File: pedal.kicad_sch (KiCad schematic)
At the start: 0 parts

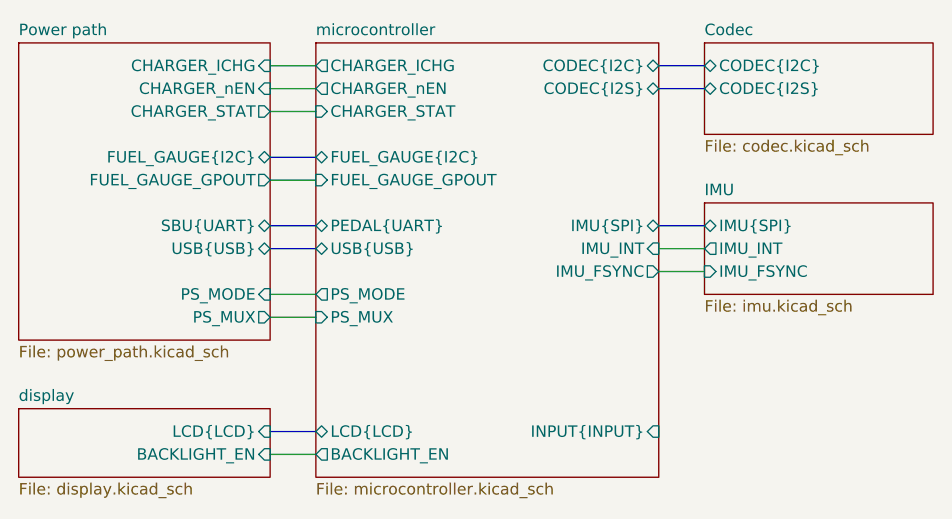
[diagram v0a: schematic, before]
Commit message: Replace output amp with TPA6130A2
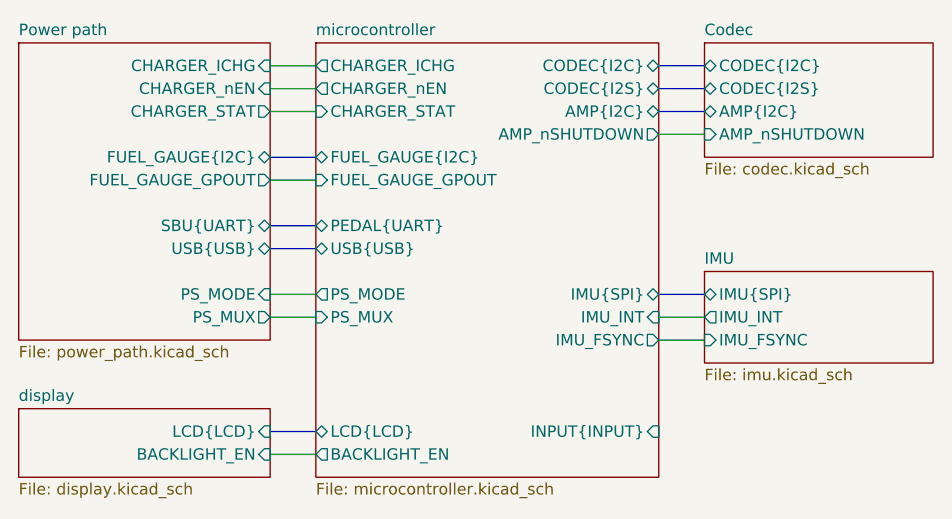
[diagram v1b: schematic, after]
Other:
- sheet Codec ports: added AMP_nSHUTDOWN, AMP{I2C}; removed none
- sheet microcontroller ports: added AMP_nSHUTDOWN, AMP{I2C}; removed none
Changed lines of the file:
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@@
 	(bus
 		(pts
-			(xy 167.64 91.44) (xy 172.72 91.44)
+			(xy 167.64 99.06) (xy 172.72 99.06)
 		)
 		(stroke
@@
 	(wire
 		(pts
-			(xy 167.64 96.52) (xy 172.72 96.52)
+			(xy 167.64 104.14) (xy 172.72 104.14)
+		)
+		(stroke
+			(width 0)
+			(type default)
+		)
+	)
+	(bus
+		(pts
+			(xy 167.64 78.74) (xy 172.72 78.74)
 		)
 		(stroke
@@
 	(wire
 		(pts
-			(xy 167.64 93.98) (xy 172.72 93.98)
+			(xy 167.64 101.6) (xy 172.72 101.6)
 		)
 		(stroke
@@
 		(pts
 			(xy 124.46 78.74) (xy 129.54 78.74)
+		)
+		(stroke
+			(width 0)
+			(type default)
+		)
+	)
+	(wire
+		(pts
+			(xy 167.64 81.28) (xy 172.72 81.28)
 		)
 		(stroke
@@
 	)
 	(sheet
-		(at 172.72 88.9)
+		(at 172.72 96.52)
 		(size 25.4 10.16)
 		(exclude_from_sim no)
@@
 		)
 		(property "Sheetname" "IMU"
-			(at 172.72 88.1884 0)
+			(at 172.72 95.8084 0)
 			(show_name no)
 			(do_not_autoplace no)
@@
 		)
 		(property "Sheetfile" "imu.kicad_sch"
-			(at 172.72 99.6446 0)
+			(at 172.72 107.2646 0)
 			(show_name no)
 			(do_not_autoplace no)
@@
 		)
 		(pin "IMU_FSYNC" input
-			(at 172.72 96.52 180)
+			(at 172.72 104.14 180)
 			(effects
 				(font
@@
 		)
 		(pin "IMU_INT" output
-			(at 172.72 93.98 180)
+			(at 172.72 101.6 180)
 			(effects
 				(font
@@
 		)
 		(pin "IMU{SPI}" bidirectional
-			(at 172.72 91.44 180)
+			(at 172.72 99.06 180)
 			(effects
 				(font
@@
 	(sheet
 		(at 172.72 71.12)
-		(size 25.4 10.16)
+		(size 25.4 12.7)
 		(exclude_from_sim no)
 		(in_bom yes)
@@
 		)
 		(property "Sheetfile" "codec.kicad_sch"
-			(at 172.72 81.8646 0)
+			(at 172.72 84.4046 0)
 			(show_name no)
 			(do_not_autoplace no)
@@
 		(pin "CODEC{I2S}" bidirectional
 			(at 172.72 76.2 180)
+			(effects
+				(font
+					(size 1.27 1.27)
+				)
+				(justify left)
+			)
+		)
+		(pin "AMP_nSHUTDOWN" input
+			(at 172.72 81.28 180)
+			(effects
+				(font
+					(size 1.27 1.27)
+				)
+				(justify left)
+			)
+		)
+		(pin "AMP{I2C}" bidirectional
+			(at 172.72 78.74 180)
 			(effects
 				(font
@@
 		)
 		(pin "IMU_FSYNC" output
-			(at 167.64 96.52 0)
+			(at 167.64 104.14 0)
 			(effects
 				(font
@@
 		)
 		(pin "IMU_INT" input
-			(at 167.64 93.98 0)
+			(at 167.64 101.6 0)
 			(effects
 				(font
@@
 		)
 		(pin "IMU{SPI}" bidirectional
-			(at 167.64 91.44 0)
+			(at 167.64 99.06 0)
 			(effects
 				(font
@@
 			)
 		)
+		(pin "AMP_nSHUTDOWN" output
+			(at 167.64 81.28 0)
+			(effects
+				(font
+					(size 1.27 1.27)
+				)
+				(justify right)
+			)
+		)
+		(pin "AMP{I2C}" bidirectional
+			(at 167.64 78.74 0)
+			(effects
+				(font
+					(size 1.27 1.27)
+				)
+				(justify right)
+			)
+		)

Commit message: FINALLY add 3.5mm audio jacks
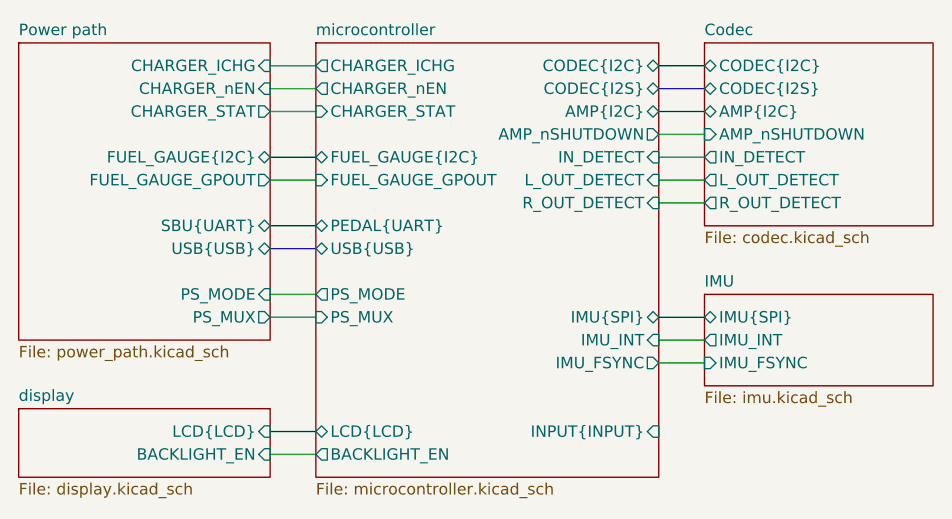
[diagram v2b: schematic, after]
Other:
- sheet Codec ports: added IN_DETECT, L_OUT_DETECT, R_OUT_DETECT; removed none
- sheet microcontroller ports: added IN_DETECT, L_OUT_DETECT, R_OUT_DETECT; removed none
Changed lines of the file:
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@@
 	(bus
 		(pts
-			(xy 167.64 99.06) (xy 172.72 99.06)
+			(xy 167.64 101.6) (xy 172.72 101.6)
 		)
 		(stroke
@@
 	(wire
 		(pts
+			(xy 167.64 106.68) (xy 172.72 106.68)
+		)
+		(stroke
+			(width 0)
+			(type default)
+		)
+	)
+	(bus
+		(pts
+			(xy 167.64 78.74) (xy 172.72 78.74)
+		)
+		(stroke
+			(width 0)
+			(type default)
+		)
+	)
+	(bus
+		(pts
+			(xy 124.46 114.3) (xy 129.54 114.3)
+		)
+		(stroke
+			(width 0)
+			(type default)
+		)
+	)
+	(wire
+		(pts
 			(xy 167.64 104.14) (xy 172.72 104.14)
 		)
@@
 		)
 	)
+	(wire
+		(pts
+			(xy 167.64 86.36) (xy 172.72 86.36)
+		)
+		(stroke
+			(width 0)
+			(type default)
+		)
+	)
 	(bus
 		(pts
-			(xy 167.64 78.74) (xy 172.72 78.74)
+			(xy 124.46 93.98) (xy 129.54 93.98)
+		)
+		(stroke
+			(width 0)
+			(type default)
+		)
+	)
+	(wire
+		(pts
+			(xy 124.46 78.74) (xy 129.54 78.74)
+		)
+		(stroke
+			(width 0)
+			(type default)
+		)
+	)
+	(wire
+		(pts
+			(xy 167.64 83.82) (xy 172.72 83.82)
+		)
+		(stroke
+			(width 0)
+			(type default)
+		)
+	)
+	(wire
+		(pts
+			(xy 167.64 81.28) (xy 172.72 81.28)
 		)
 		(stroke
@@
 	(bus
 		(pts
-			(xy 124.46 114.3) (xy 129.54 114.3)
-		)
-		(stroke
-			(width 0)
-			(type default)
-		)
-	)
-	(wire
-		(pts
-			(xy 167.64 101.6) (xy 172.72 101.6)
+			(xy 167.64 76.2) (xy 172.72 76.2)
 		)
 		(stroke
@@
 	(bus
 		(pts
-			(xy 124.46 93.98) (xy 129.54 93.98)
-		)
-		(stroke
-			(width 0)
-			(type default)
-		)
-	)
-	(wire
-		(pts
-			(xy 124.46 78.74) (xy 129.54 78.74)
-		)
-		(stroke
-			(width 0)
-			(type default)
-		)
-	)
-	(wire
-		(pts
-			(xy 167.64 81.28) (xy 172.72 81.28)
-		)
-		(stroke
-			(width 0)
-			(type default)
-		)
-	)
-	(bus
-		(pts
-			(xy 167.64 76.2) (xy 172.72 76.2)
-		)
-		(stroke
-			(width 0)
-			(type default)
-		)
-	)
-	(bus
-		(pts
 			(xy 124.46 91.44) (xy 129.54 91.44)
 		)
@@
 		(pts
 			(xy 124.46 86.36) (xy 129.54 86.36)
+		)
+		(stroke
+			(width 0)
+			(type default)
+		)
+	)
+	(wire
+		(pts
+			(xy 167.64 88.9) (xy 172.72 88.9)
 		)
 		(stroke
@@
 	)
 	(sheet
-		(at 172.72 96.52)
+		(at 172.72 99.06)
 		(size 25.4 10.16)
 		(exclude_from_sim no)
@@
 		)
 		(property "Sheetname" "IMU"
-			(at 172.72 95.8084 0)
+			(at 172.72 98.3484 0)
 			(show_name no)
 			(do_not_autoplace no)
@@
 		)
 		(property "Sheetfile" "imu.kicad_sch"
-			(at 172.72 107.2646 0)
+			(at 172.72 109.8046 0)
 			(show_name no)
 			(do_not_autoplace no)
@@
 		)
 		(pin "IMU_FSYNC" input
+			(at 172.72 106.68 180)
+			(effects
+				(font
+					(size 1.27 1.27)
+				)
+				(justify left)
+			)
+		)
+		(pin "IMU_INT" output
 			(at 172.72 104.14 180)
 			(effects
@@
 			)
 		)
-		(pin "IMU_INT" output
+		(pin "IMU{SPI}" bidirectional
 			(at 172.72 101.6 180)
-			(effects
-				(font
-					(size 1.27 1.27)
-				)
-				(justify left)
-			)
-		)
-		(pin "IMU{SPI}" bidirectional
-			(at 172.72 99.06 180)
 			(effects
 				(font
@@
 	(sheet
 		(at 172.72 71.12)
-		(size 25.4 12.7)
+		(size 25.4 20.32)
 		(exclude_from_sim no)
 		(in_bom yes)
@@
 		)
 		(property "Sheetfile" "codec.kicad_sch"
-			(at 172.72 84.4046 0)
+			(at 172.72 92.0246 0)
 			(show_name no)
 			(do_not_autoplace no)
@@
 		(pin "AMP{I2C}" bidirectional
 			(at 172.72 78.74 180)
+			(effects
+				(font
+					(size 1.27 1.27)
+				)
+				(justify left)
+			)
+		)
+		(pin "IN_DETECT" output
+			(at 172.72 83.82 180)
+			(effects
+				(font
+					(size 1.27 1.27)
+				)
+				(justify left)
+			)
+		)
+		(pin "L_OUT_DETECT" output
+			(at 172.72 86.36 180)
+			(effects
+				(font
+					(size 1.27 1.27)
+				)
+				(justify left)
+			)
+		)
+		(pin "R_OUT_DETECT" output
+			(at 172.72 88.9 180)
 			(effects
 				(font
@@
 		)
 		(pin "IMU_FSYNC" output
+			(at 167.64 106.68 0)
+			(effects
+				(font
+					(size 1.27 1.27)
+				)
+				(justify right)
+			)
+		)
+		(pin "IMU_INT" input
 			(at 167.64 104.14 0)
 			(effects
@@
 			)
 		)
-		(pin "IMU_INT" input
+		(pin "IMU{SPI}" bidirectional
 			(at 167.64 101.6 0)
-			(effects
-				(font
-					(size 1.27 1.27)
-				)
-				(justify right)
-			)
-		)
-		(pin "IMU{SPI}" bidirectional
-			(at 167.64 99.06 0)
 			(effects
 				(font
@@
 			(effects
 				(font
+					(size 1.27 1.27)
+				)
+				(justify right)
+			)
+		)
+		(pin "IN_DETECT" input
+			(at 167.64 83.82 0)
+			(effects
+				(font
+					(size 1.27 1.27)
+				)
+				(justify right)
+			)
+		)
+		(pin "L_OUT_DETECT" input
+			(at 167.64 86.36 0)
+			(effects
+				(font
+					(size 1.27 1.27)
+				)
+				(justify right)
+			)
+		)
+		(pin "R_OUT_DETECT" input
+			(at 167.64 88.9 0)
+			(effects
+				(font

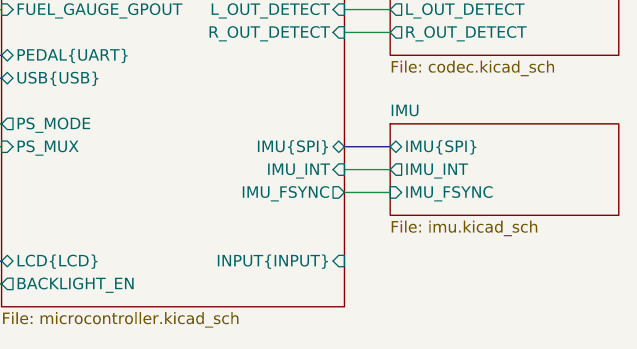
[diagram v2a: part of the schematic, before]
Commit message: Input (#6)
* Add input subsheet
* Add debounce subsheet
* Add ultra thin buttons for ABXY
* Add start and select buttons
* Add L/R buttons
* Add joystick connector
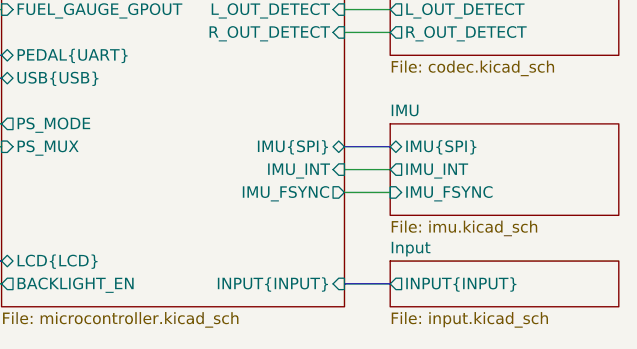
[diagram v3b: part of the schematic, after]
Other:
- added sheet Input (input.kicad_sch)
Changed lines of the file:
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@@
 	(bus
 		(pts
+			(xy 167.64 116.84) (xy 172.72 116.84)
+		)
+		(stroke
+			(width 0)
+			(type default)
+		)
+	)
+	(bus
+		(pts
 			(xy 124.46 93.98) (xy 129.54 93.98)
 		)
@@
 			(width 0)
 			(type default)
+		)
+	)
+	(sheet
+		(at 172.72 114.3)
+		(size 25.4 5.08)
+		(exclude_from_sim no)
+		(in_bom yes)
+		(on_board yes)
+		(dnp no)
+		(fields_autoplaced yes)
+		(stroke
+			(width 0.1524)
+			(type solid)
+		)
+		(fill
+			(color 0 0 0 0)
+		)
+		(property "Sheetname" "Input"
+			(at 172.72 113.5884 0)
+			(show_name no)
+			(do_not_autoplace no)
+			(effects
+				(font
+					(size 1.27 1.27)
+				)
+				(justify left bottom)
+			)
+		)
+		(property "Sheetfile" "input.kicad_sch"
+			(at 172.72 119.9646 0)
+			(show_name no)
+			(do_not_autoplace no)
+			(effects
+				(font
+					(size 1.27 1.27)
+				)
+				(justify left top)
+			)
+		)
+		(pin "INPUT{INPUT}" output
+			(at 172.72 116.84 180)
+			(effects
+				(font
+					(size 1.27 1.27)
+				)
+				(justify left)
+			)
+		)
+		(instances
+			(project "pedal"
+				(path "/e2443317-b83f-4e66-ac79-3186c6d613f3"
+					(page "8")
+				)
+			)
 		)
 	)
@@
 		)
 		(pin "INPUT{INPUT}" input
-			(at 167.64 114.3 0)
-			(effects
-				(font
+			(at 167.64 116.84 0)
+			(effects
+				(font
